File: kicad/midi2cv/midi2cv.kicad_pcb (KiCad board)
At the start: 2 copper layers, 81.3 x 96.5 mm, 61 parts, among them J1 ProgramJmpr, J10 CTL1 Output, J11 CTL2 Output, J12 Gate1 Output, J13 Gate2 Output, J14 Conn_01x08_Male, J15 Conn_01x08_Female, J16 P1, J17 P2, J18 P3, J19 P4, J2 Power, J20 P5, J21 P6, J22 P7, J23 P8, J3 Conn_01x04_Male, J4 Conn_01x04_Female, J5 Conn_01x08_Male, J6 Conn_01x08_Female, J7 Midi Input, J8 CV1 Output, J9 CV2 Output, U1 L7805, U2 24LC256, U3 MCP4922, U4 MCP4922, U5 PC817, U6 TL074, U7 74HC595, U8 TL074

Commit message: Create pcb.
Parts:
- added J24: Conn_01x04_Female, Connector_PinHeader_2.54mm:PinHeader_1x04_P2.54mm_Vertical, B.Cu at (73.4, 32.8)
- added J25: Conn_01x04_Female, Connector_PinHeader_2.54mm:PinHeader_1x04_P2.54mm_Vertical, B.Cu at (101.9, 32.8)
- J14: value Conn_01x08_Male -> Conn_01x04_Male; footprint Connector_PinSocket_2.54mm:PinSocket_1x08_P2.54mm_Vertical -> Connector_PinSocket_2.54mm:PinSocket_1x04_P2.54mm_Vertical
- J15: value Conn_01x08_Female -> Conn_01x04_Male; footprint Connector_PinHeader_2.54mm:PinHeader_1x08_P2.54mm_Vertical -> Connector_PinSocket_2.54mm:PinSocket_1x04_P2.54mm_Vertical; moved to F.Cu
- moved C8 30.8 mm to (66.5, 46.7), turned to 90 degrees
- moved C6 28.8 mm to (37.1, 46.7), turned to 90 degrees
- moved J3 26.5 mm to (32.8, 36.8), turned to 0 degrees
- moved J4 26.5 mm to (73.4, 36.8), turned to 180 degrees
- moved D1 25.5 mm to (80.0, 39.4)
- moved U6 23.3 mm to (46.5, 36.6), turned to 180 degrees
- moved R3 17.9 mm to (83.1, 43.9), turned to 90 degrees
- moved C4 16.6 mm to (65.5, 101.6), turned to 180 degrees
- moved U8 16.4 mm to (62.7, 36.6), turned to 180 degrees
- moved C3 16.1 mm to (55.0, 101.6), turned to 180 degrees
- moved U3 15.9 mm to (69.2, 106.0), turned to 180 degrees
- moved J15 14.5 mm to (61.2, 32.8), turned to 90 degrees
- moved C2 10.5 mm to (65.0, 87.4)
- moved C1 10.3 mm to (55.1, 87.4)
- moved RV1 9.26 mm to (94.0, 47.0), turned to 90 degrees
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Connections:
- R10 pad 1: Net-(J15-Pad6) -> Net-(J24-Pad2)
- R11 pad 1: Net-(J15-Pad5) -> Net-(J24-Pad1)
- R12 pad 1: Net-(J15-Pad4) -> Net-(J25-Pad4)
- R13 pad 1: Net-(J15-Pad3) -> Net-(J25-Pad3)
- R14 pad 1: Net-(J15-Pad2) -> Net-(J25-Pad2)
- R15 pad 1: Net-(J15-Pad1) -> Net-(J25-Pad1)
- R8 pad 1: Net-(J15-Pad8) -> Net-(J24-Pad4)
- R9 pad 1: Net-(J15-Pad7) -> Net-(J24-Pad3)
- U6 pad 1: Net-(J14-Pad8) -> Net-(J14-Pad4)
- U6 pad 13: Net-(J14-Pad5) -> Net-(J14-Pad1)
- U6 pad 14: Net-(J14-Pad5) -> Net-(J14-Pad1)
- U6 pad 2: Net-(J14-Pad8) -> Net-(J14-Pad4)
- U6 pad 6: Net-(J14-Pad7) -> Net-(J14-Pad3)
- U6 pad 7: Net-(J14-Pad7) -> Net-(J14-Pad3)
- U6 pad 8: Net-(J14-Pad6) -> Net-(J14-Pad2)
- U6 pad 9: Net-(J14-Pad6) -> Net-(J14-Pad2)
- U8 pad 1: Net-(J14-Pad4) -> Net-(J15-Pad4)
- U8 pad 13: Net-(J14-Pad1) -> Net-(J15-Pad1)
- U8 pad 14: Net-(J14-Pad1) -> Net-(J15-Pad1)
- U8 pad 2: Net-(J14-Pad4) -> Net-(J15-Pad4)
- U8 pad 6: Net-(J14-Pad3) -> Net-(J15-Pad3)
- U8 pad 7: Net-(J14-Pad3) -> Net-(J15-Pad3)
- U8 pad 8: Net-(J14-Pad2) -> Net-(J15-Pad2)
- U8 pad 9: Net-(J14-Pad2) -> Net-(J15-Pad2)
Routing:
- net Net-(J25-Pad2): track 0.00 -> 75.2 mm
- net Net-(J25-Pad1): track 0.00 -> 66.4 mm
- net Net-(J25-Pad4): track 0.00 -> 64.1 mm, vias 0 -> 1
- net Net-(J25-Pad3): track 0.00 -> 63.2 mm
- net Net-(J15-Pad1): track 63.2 -> 10.2 mm, vias 1 -> 0
- net Net-(J15-Pad2): track 70.3 -> 23.3 mm
- net Net-(J24-Pad1): track 0.00 -> 46.8 mm, vias 0 -> 1
- net GND: track 3.66 -> 47.0 mm, vias 0 -> 2
- net Net-(J15-Pad3): track 67.5 -> 24.4 mm
- net Net-(J15-Pad5): track 41.0 -> 0.00 mm
- net Net-(J15-Pad4): track 47.8 -> 10.2 mm
- net Net-(J24-Pad2): track 0.00 -> 37.1 mm
- net Net-(J24-Pad3): track 0.00 -> 36.9 mm, vias 0 -> 1
- net Net-(J15-Pad6): track 33.2 -> 0.00 mm
- net Net-(U7-Pad6): track 50.7 -> 18.8 mm, vias 2 -> 0
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- added copper zone on F.Cu, net GND
- added copper zone on F.Cu, net GNDA

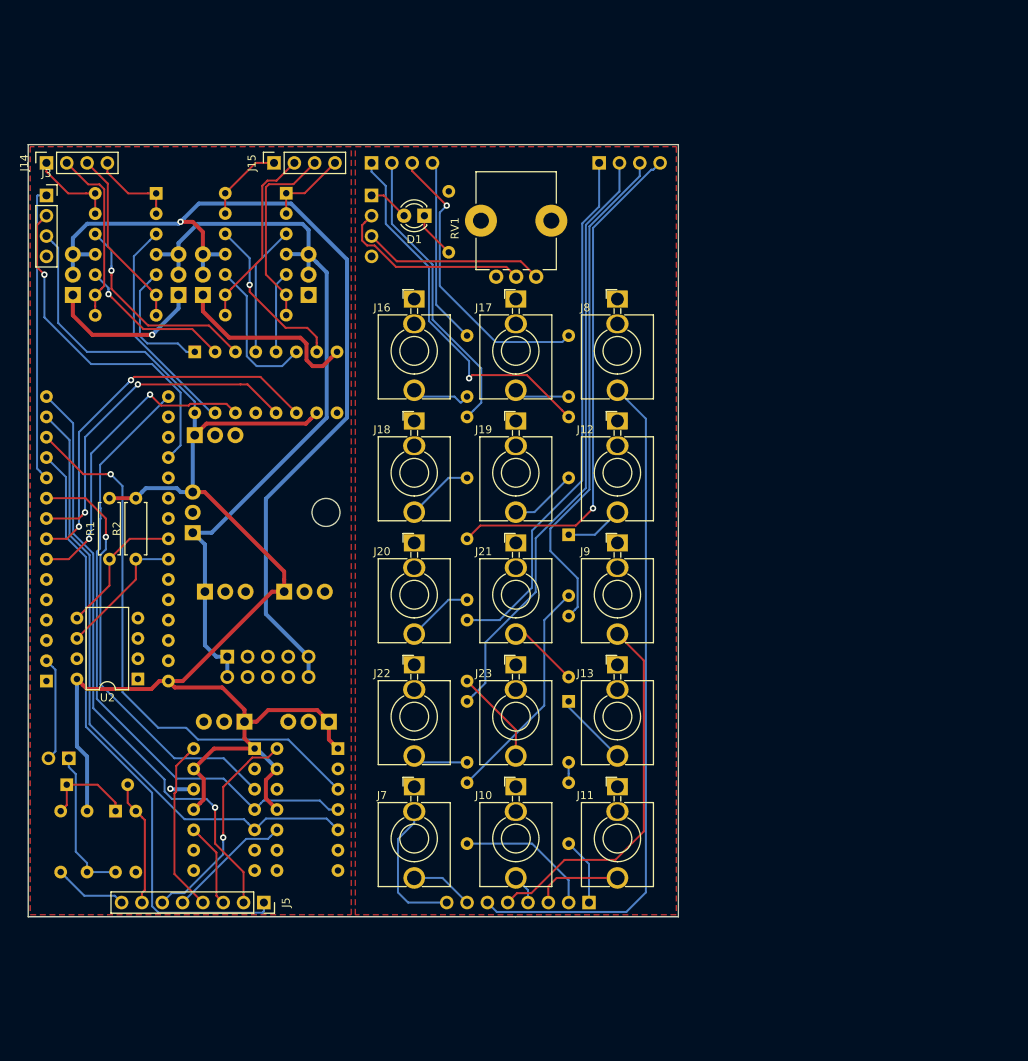
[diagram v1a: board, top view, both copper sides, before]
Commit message: Add frontpanel.
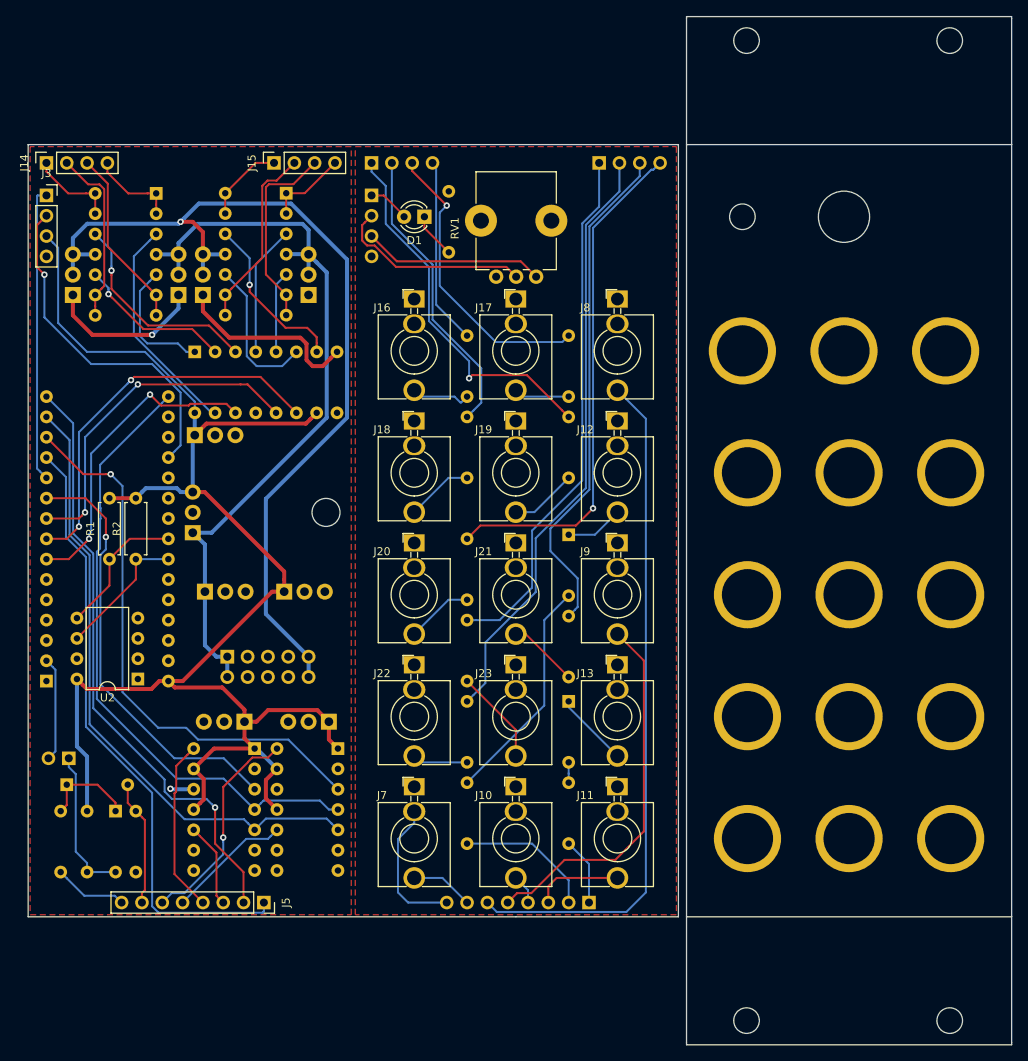
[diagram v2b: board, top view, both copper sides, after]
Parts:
- added REF**: MountingHole_6.4mm_M6, MountingHole:MountingHole_6.4mm_M6, F.Cu at (132.5, 39.5)
- added REF**: MountingHole_6.4mm_M6_Pad, MountingHole:MountingHole_6.4mm_M6_Pad, F.Cu at (145.8, 86.7)
- added REF**: MountingHole_6.4mm_M6_Pad, MountingHole:MountingHole_6.4mm_M6_Pad, F.Cu at (120.4, 86.7)
- added REF**: MountingHole_6.4mm_M6_Pad, MountingHole:MountingHole_6.4mm_M6_Pad, F.Cu at (133.1, 102.0)
- added REF**: MountingHole_6.4mm_M6_Pad, MountingHole:MountingHole_6.4mm_M6_Pad, F.Cu at (145.8, 102.0)
- added REF**: MountingHole_6.4mm_M6_Pad, MountingHole:MountingHole_6.4mm_M6_Pad, F.Cu at (120.4, 102.0)
- added REF**: MountingHole_6.4mm_M6_Pad, MountingHole:MountingHole_6.4mm_M6_Pad, F.Cu at (145.8, 117.2)
- added REF**: MountingHole_6.4mm_M6_Pad, MountingHole:MountingHole_6.4mm_M6_Pad, F.Cu at (133.1, 117.2)
- added REF**: MountingHole_3.2mm_M3, MountingHole:MountingHole_3.2mm_M3, F.Cu at (120.3, 17.5)
- added REF**: MountingHole_3.2mm_M3, MountingHole:MountingHole_3.2mm_M3, F.Cu at (145.7, 17.5)
- added REF**: MountingHole_3.2mm_M3, MountingHole:MountingHole_3.2mm_M3, F.Cu at (145.7, 140.0)
- added REF**: MountingHole_3.2mm_M3, MountingHole:MountingHole_3.2mm_M3, F.Cu at (119.8, 39.5)
- added REF**: MountingHole_3.2mm_M3, MountingHole:MountingHole_3.2mm_M3, F.Cu at (120.3, 140.0)
- added REF**: MountingHole_6.4mm_M6_Pad, MountingHole:MountingHole_6.4mm_M6_Pad, F.Cu at (120.4, 117.2)
- added REF**: MountingHole_6.4mm_M6_Pad, MountingHole:MountingHole_6.4mm_M6_Pad, F.Cu at (119.8, 56.3)
- added REF**: MountingHole_6.4mm_M6_Pad, MountingHole:MountingHole_6.4mm_M6_Pad, F.Cu at (145.2, 56.3)
- added REF**: MountingHole_6.4mm_M6_Pad, MountingHole:MountingHole_6.4mm_M6_Pad, F.Cu at (132.5, 56.3)
- added REF**: MountingHole_6.4mm_M6_Pad, MountingHole:MountingHole_6.4mm_M6_Pad, F.Cu at (133.1, 71.5)
- added REF**: MountingHole_6.4mm_M6_Pad, MountingHole:MountingHole_6.4mm_M6_Pad, F.Cu at (145.8, 71.5)
- added REF**: MountingHole_6.4mm_M6_Pad, MountingHole:MountingHole_6.4mm_M6_Pad, F.Cu at (120.4, 71.5)
- added REF**: MountingHole_6.4mm_M6_Pad, MountingHole:MountingHole_6.4mm_M6_Pad, F.Cu at (133.1, 86.7)
- moved D1 0.13 mm to (80.0, 39.5)
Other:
- board size 81.3 x 96.5 mm -> 122.9 x 128.5 mm

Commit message: Update some symbols + footprints.
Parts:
- removed REF**: MountingHole_6.4mm_M6, MountingHole:MountingHole_6.4mm_M6
- removed REF** (x15): MountingHole_6.4mm_M6_Pad, MountingHole:MountingHole_6.4mm_M6_Pad
- removed REF** (x5): MountingHole_3.2mm_M3, MountingHole:MountingHole_3.2mm_M3
- A1: footprint Module:Arduino_Nano -> Tomarus:Arduino_Nano_Silk
- moved RV1 5.08 mm to (94.0, 41.9)
- moved D1 4.19 mm to (80.0, 35.3)
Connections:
- A1 pad 27: Net-(A1-Pad27) -> +5V
- A1 pad 30: +5V -> Net-(A1-Pad30)
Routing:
- net GND: track 47.0 -> 67.7 mm, vias 2 -> 3
- net +5V: track 195.0 -> 205.6 mm
- net Net-(J4-Pad2): track 24.7 -> 20.4 mm
- net Net-(D1-Pad1): track 5.71 -> 9.90 mm, vias 0 -> 1
- net Net-(J24-Pad3): track 36.9 -> 37.7 mm
- net GATE2_OUT: track 77.0 -> 77.7 mm
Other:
- board size 122.9 x 128.5 mm -> 81.3 x 96.5 mm

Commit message: Small production updates.
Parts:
- RV1: footprint Potentiometer_THT:Potentiometer_Alps_RK09K_Single_Vertical -> Tomarus:Potentiometer_Alps_RK09K_Single_Vertical_HalfSilk
- renumbered A1 to NANO
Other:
- outline, holes or cut-outs redrawn

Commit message: Fix a gnd connection.
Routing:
- net GND: track 67.7 -> 74.3 mm
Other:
- board text added: "JLCJLCJLCJLC"
- board text added: "TOMARUS Miarph v1.0"
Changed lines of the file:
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@@
   (general
     (thickness 1.6)
-    (drawings 10)
-    (tracks 564)
+    (drawings 12)
+    (tracks 566)
     (zones 0)
     (modules 63)
@@
   )
   (setup
-    (last_trace_width 0.25)
+    (last_trace_width 0.5)
     (user_trace_width 0.5)
     (trace_clearance 0.2)
@@
     (visible_elements FFFFFF7F)
     (pcbplotparams
-      (layerselection 0x010f0_ffffffff)
+      (layerselection 0x014f0_ffffffff)
       (usegerberextensions false)
       (usegerberattributes false)
@@
     )
   )
+  (gr_text JLCJLCJLCJLC (at 64.262 72.898) (layer F.SilkS)
+    (effects (font (size 1 1) (thickness 0.15)))
+  )
+  (gr_text "TOMARUS\nMiarph v1.0" (at 64.008 69.088) (layer F.SilkS)
+    (effects (font (size 1.5 1.5) (thickness 0.3)))
+  )
   (gr_line (start 71.12 30.48) (end 71.12 127) (layer Edge.Cuts) (width 0.15))
   (gr_line (start 111.76 30.48) (end 91.44 30.48) (layer Edge.Cuts) (width 0.15))
@@
   (segment (start 43.942 121.412) (end 45.683032 121.412) (width 0.5) (layer B.Cu) (net 7))
   (segment (start 48.006 121.158) (end 45.937032 121.158) (width 0.5) (layer F.Cu) (net 7))
+  (segment (start 60.452 100.076) (end 60.452 97.028) (width 0.5) (layer B.Cu) (net 7))
+  (segment (start 62.992 102.616) (end 60.452 100.076) (width 0.5) (layer B.Cu) (net 7))
   (via (at 45.72 61.722) (size 0.8) (drill 0.4) (layers F.Cu B.Cu) (net 13))
   (segment (start 47.099001 63.101001) (end 45.72 61.722) (width 0.25) (layer F.Cu) (net 13))

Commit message: Fix caps silkscreen + powerconnector.
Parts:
- removed NANO: Nano v3, Tomarus:Arduino_Nano_Silk
- added A1: Arduino_Nano_v3.x, Tomarus:Arduino_Nano_Silk, B.Cu at (32.8, 97.5)
- R3: value 1K -> 10K
- moved J2 10.5 mm to (65.5, 97.0), turned to 90 degrees
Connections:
- J2 pad 1: +12V -> -12V
- J2 pad 10: -12V -> +12V
- J2 pad 2: +12V -> -12V
- J2 pad 9: -12V -> +12V
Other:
- board text added: "TOMARUS Miarph v1.1"
- board text removed: "TOMARUS Miarph v1.0"

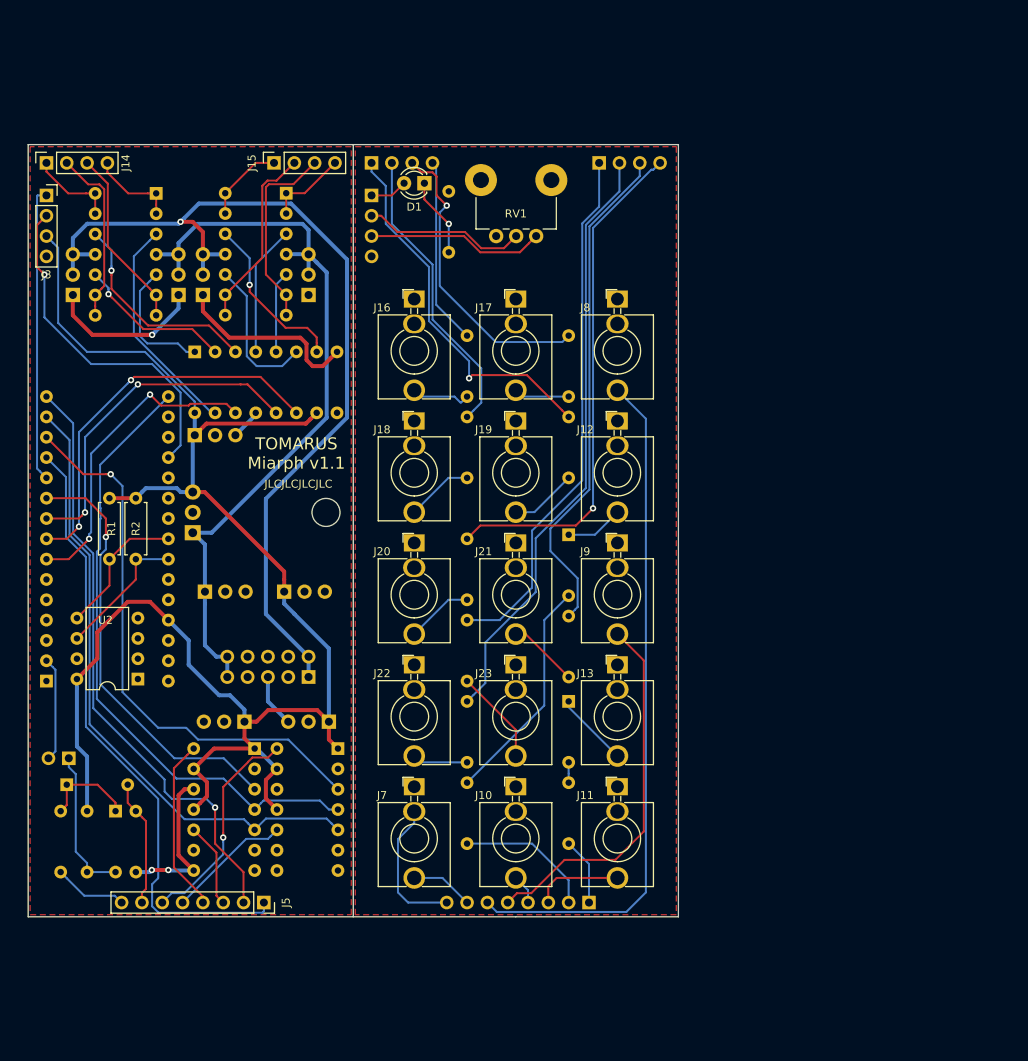
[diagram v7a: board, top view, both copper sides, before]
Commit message: Make trigger ports configurable as either drum trigger or clock divider.
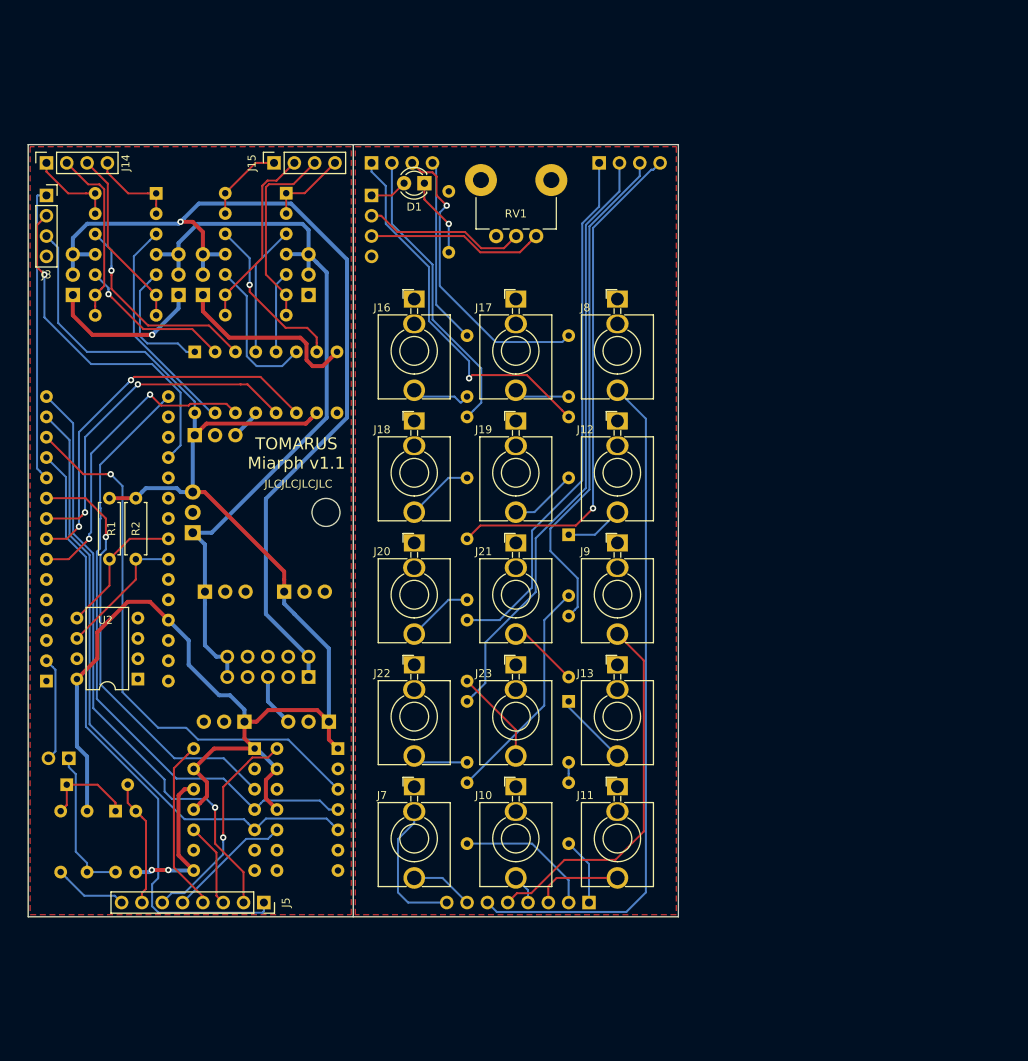
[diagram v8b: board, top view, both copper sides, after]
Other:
- outline, holes or cut-outs redrawn
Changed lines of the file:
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@@
   (general
     (thickness 1.6)
-    (drawings 12)
+    (drawings 10)
     (tracks 566)
     (zones 0)
@@
     )
   )
+  (gr_line (start 71.12 30.48) (end 71.12 127) (layer Edge.Cuts) (width 0.15))
   (gr_text JLCJLCJLCJLC (at 64.262 72.898) (layer F.SilkS)
     (effects (font (size 1 1) (thickness 0.15)))
@@
     (effects (font (size 1.5 1.5) (thickness 0.3)))
   )
-  (gr_line (start 71.12 30.48) (end 71.12 127) (layer Edge.Cuts) (width 0.15))
-  (gr_line (start 111.76 30.48) (end 91.44 30.48) (layer Edge.Cuts) (width 0.15))
-  (gr_line (start 111.76 127) (end 91.44 127) (layer Edge.Cuts) (width 0.15))
   (gr_text V-Cut (at 71.12 23.368) (layer Eco1.User)
     (effects (font (size 1.5 1.5) (thickness 0.3)))
@@
   )
   (gr_line (start 71.12 25.4) (end 71.12 132.08) (layer Eco1.User) (width 0.15))
-  (gr_line (start 91.44 30.48) (end 30.48 30.48) (layer Edge.Cuts) (width 0.15))
+  (gr_line (start 111.76 30.48) (end 30.48 30.48) (layer Edge.Cuts) (width 0.15))
   (gr_line (start 111.76 127) (end 111.76 30.48) (layer Edge.Cuts) (width 0.15))
-  (gr_line (start 30.48 127) (end 91.44 127) (layer Edge.Cuts) (width 0.15))
+  (gr_line (start 30.48 127) (end 111.76 127) (layer Edge.Cuts) (width 0.15))
   (gr_line (start 30.48 30.48) (end 30.48 127) (layer Edge.Cuts) (width 0.15))
   (segment (start 33.565999 95.795999) (end 32.766 94.996) (width 0.25) (layer B.Cu) (net 3))
